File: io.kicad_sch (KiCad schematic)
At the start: 39 parts, among them J10 RIGHT WHEEL SENS, J11 STARTER CON, J12 USB_C_Receptacle, J13 USB_C_Receptacle, J14 CAN, J15 3.3V OUT, J16 5V OUT, J17 7.5V OUT, J18 OIL CON, J19 IAT CON, J20 PRIM TRIGG CON, J21 SEC TRIGG CON, J22 EGT CON, J23 DATA LOGGER CON, J24 IGN CON, J25 INJ CON, J26 MAP, J27 CLT CON, J3 EMU_BLACK_A, J4 EMU_BLACK_B, J6 INJ_&_STARTER, J7 16V OUT, J8 SERVO, J9 LEFT WHEEL SENS, K1 FINDER-34.51 INJ, K2 FINDER-34.51 STARTER, K3 FINDER-34.51 INJ, Q2 IRFP1405PBF, Q3 IRFP1405PBF, Q4 IRFP1405PBF, U7 TXS0108EPWR, U8 2EDN7524F

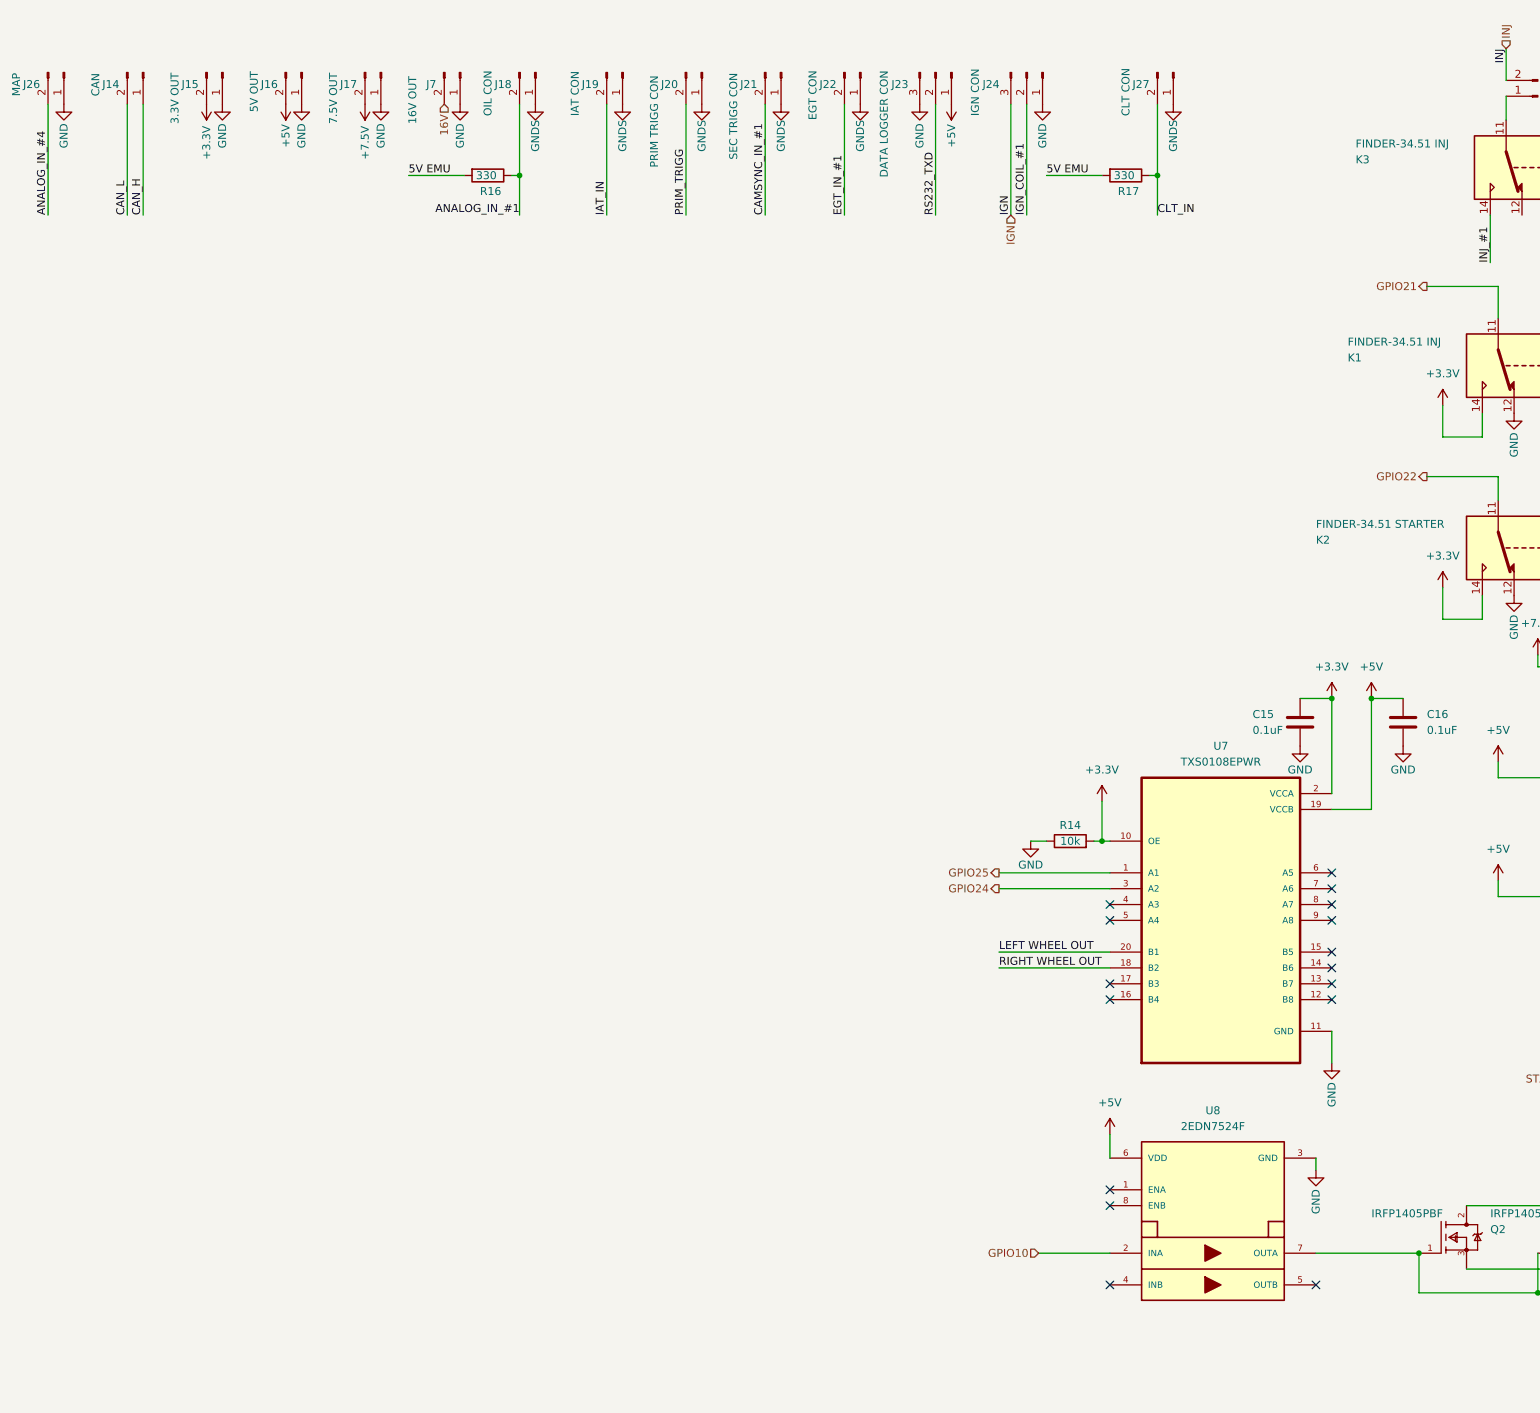
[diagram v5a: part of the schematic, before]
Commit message: Added CAN transsiver to RP2040
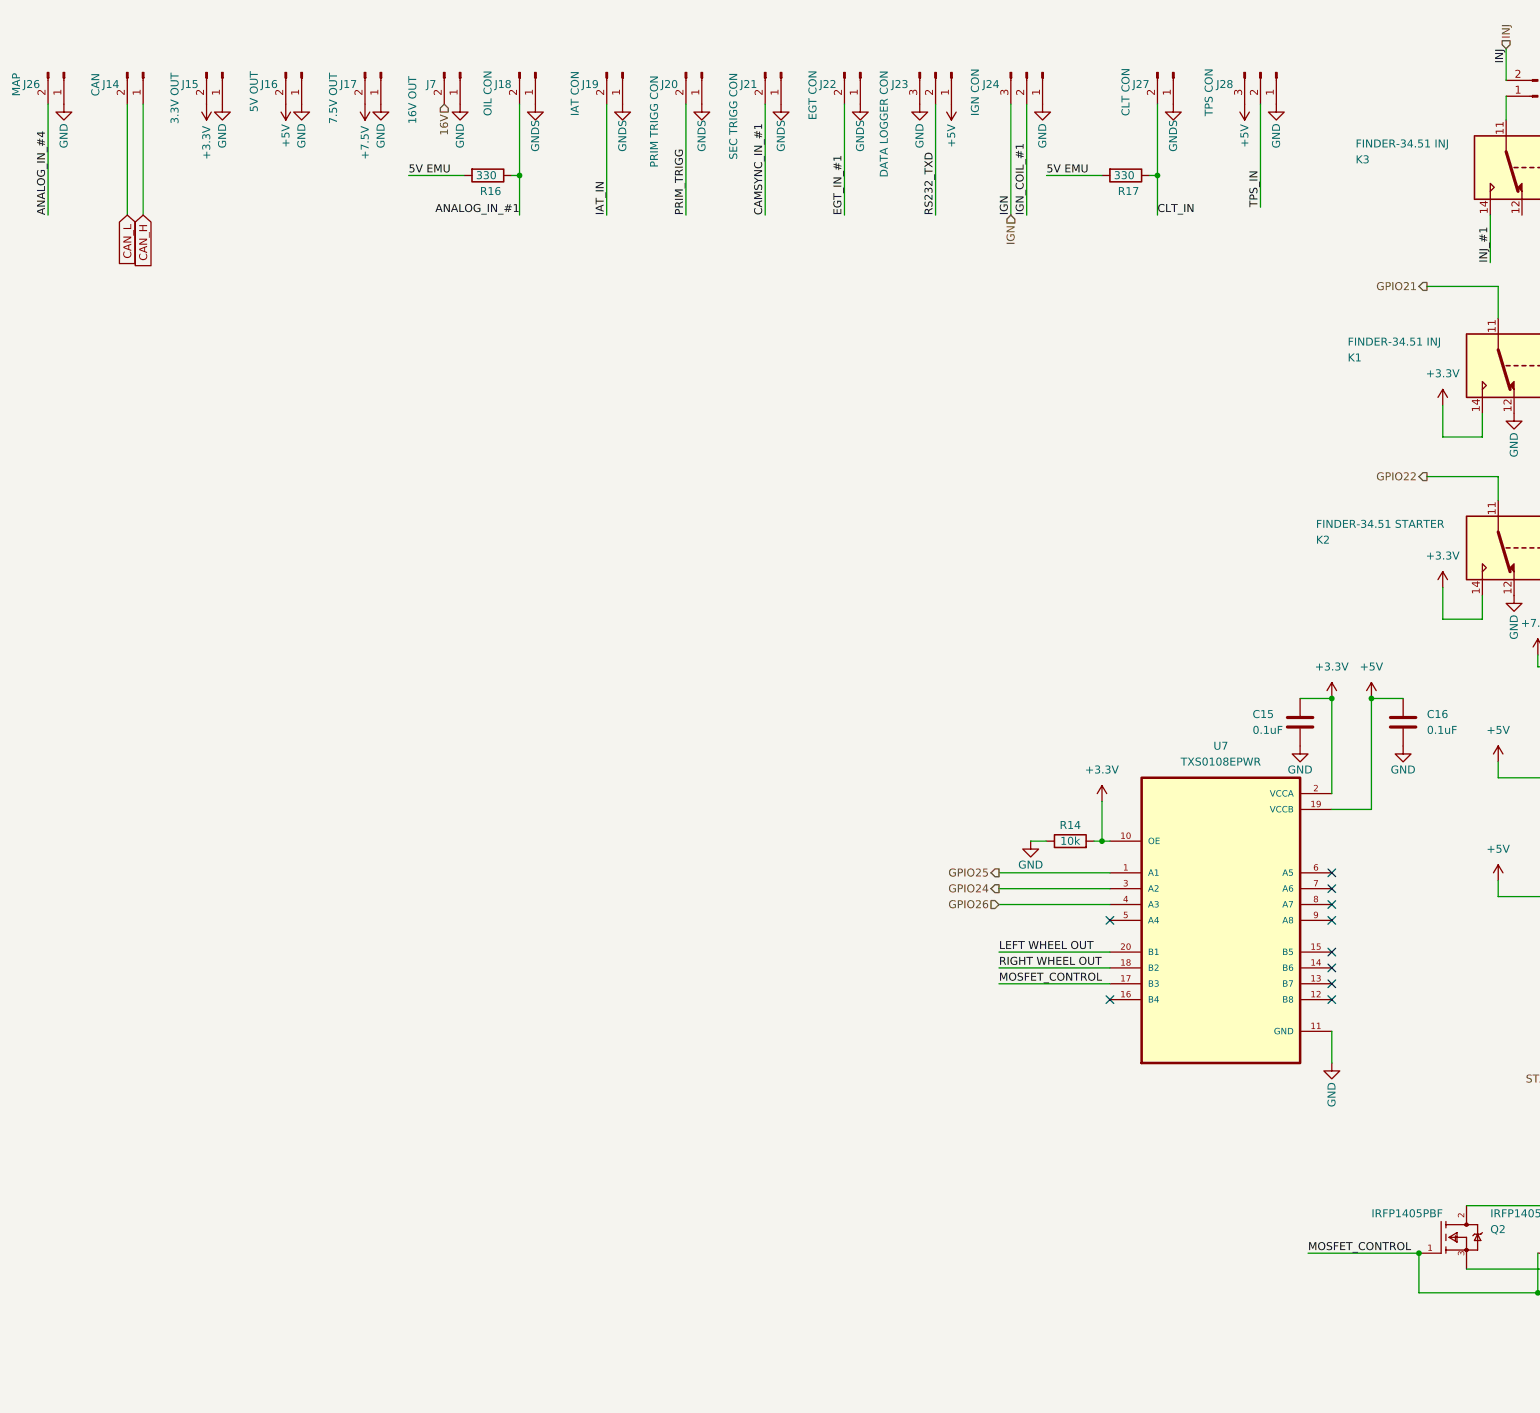
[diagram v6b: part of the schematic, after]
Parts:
- removed U8: 2EDN7524F, 2EDN7524F:SOIC127P600X175-8N-22-V, symbol 2EDN7524F:2EDN7524F
- added J28: TPS CON, TerminalBlock_Phoenix:TerminalBlock_Phoenix_MPT-0,5-3-2.54_1x03_P2.54mm_Horizontal, symbol Connector:Conn_01x03_Male
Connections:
- net +5V: now also J28.3 (Pin_3)
- net GND: now also J28.1 (Pin_1)
- net TPS_IN: now also J28.2 (Pin_2)
- net MOSFET_CONTROL: now reaches U7.17 (B3)
- net MOSFET_CONTROL: now also Q2.1 (G), Q3.1 (G), Q4.1 (G)
- net GPIO26: now reaches U7.4 (A3)
- no-connect marks 42 -> 36
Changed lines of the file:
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@@
   (no_connect (at 46.99 154.94))
   (no_connect (at 46.99 213.36))
-  (no_connect (at 290.83 214.63))
   (no_connect (at 46.99 144.78))
   (no_connect (at 290.83 168.91))
@@
   (no_connect (at 290.83 156.21))
   (no_connect (at 46.99 152.4))
-  (no_connect (at 323.85 214.63))
   (no_connect (at 46.99 147.32))
   (no_connect (at 46.99 139.7))
-  (no_connect (at 290.83 166.37))
   (no_connect (at 46.99 180.34))
   (no_connect (at 46.99 231.14))
   (no_connect (at 326.39 161.29))
-  (no_connect (at 290.83 201.93))
-  (no_connect (at 290.83 199.39))
   (no_connect (at 375.92 189.23))
   (no_connect (at 46.99 137.16))
-  (no_connect (at 290.83 153.67))
   (no_connect (at 326.39 166.37))
   (wire (pts (xy 102.87 68.58) (xy 102.87 50.8))
@@
     (stroke (width 0) (type default) (color 0 0 0 0))
   )
-  (wire (pts (xy 279.4 209.55) (xy 290.83 209.55))
-    (stroke (width 0) (type default) (color 0 0 0 0))
-  )
   (wire (pts (xy 54.61 68.58) (xy 54.61 50.8))
     (stroke (width 0) (type default) (color 0 0 0 0))
@@
     (stroke (width 0) (type default) (color 0 0 0 0))
   )
+  (wire (pts (xy 273.05 166.37) (xy 290.83 166.37))
+    (stroke (width 0) (type default) (color 0 0 0 0))
+  )
   (wire (pts (xy 90.17 20.32) (xy 90.17 38.1))
     (stroke (width 0) (type default) (color 0 0 0 0))
@@
     (stroke (width 0) (type default) (color 0 0 0 0))
   )
-  (wire (pts (xy 323.85 209.55) (xy 340.36 209.55))
+  (wire (pts (xy 322.58 209.55) (xy 340.36 209.55))
     (stroke (width 0) (type default) (color 0 0 0 0))
   )
@@
     (stroke (width 0) (type default) (color 0 0 0 0))
   )
+  (wire (pts (xy 273.05 153.67) (xy 290.83 153.67))
+    (stroke (width 0) (type default) (color 0 0 0 0))
+  )
   (wire (pts (xy 110.49 20.32) (xy 110.49 38.1))
     (stroke (width 0) (type default) (color 0 0 0 0))
@@
     (stroke (width 0) (type default) (color 0 0 0 0))
   )
-  (wire (pts (xy 290.83 190.5) (xy 290.83 194.31))
-    (stroke (width 0) (type default) (color 0 0 0 0))
-  )
   (wire (pts (xy 46.99 114.3) (xy 46.99 116.84))
     (stroke (width 0) (type default) (color 0 0 0 0))
@@
     (stroke (width 0) (type default) (color 0 0 0 0))
   )
-  (wire (pts (xy 323.85 196.215) (xy 323.85 194.31))
-    (stroke (width 0) (type default) (color 0 0 0 0))
-  )
   (wire (pts (xy 359.41 115.57) (xy 381 115.57))
     (stroke (width 0) (type default) (color 0 0 0 0))
@@
     (stroke (width 0) (type default) (color 0 0 0 0))
   )
+  (wire (pts (xy 314.96 41.91) (xy 314.96 25.4))
+    (stroke (width 0) (type default) (color 0 0 0 0))
+  )
   (wire (pts (xy 178.435 36.83) (xy 187.325 36.83))
     (stroke (width 0) (type default) (color 0 0 0 0))
@@
     (effects (font (size 1.27 1.27)) (justify right bottom))
   )
+  (label "MOSFET_CONTROL" (at 273.05 166.37 0)
+    (effects (font (size 1.27 1.27)) (justify left bottom))
+  )
   (label "RIGHT WHEEL OUT" (at 273.05 163.83 0)
     (effects (font (size 1.27 1.27)) (justify left bottom))
@@
     (effects (font (size 1.27 1.27)) (justify left bottom))
   )
+  (label "TPS_IN" (at 314.96 41.91 90)
+    (effects (font (size 1.27 1.27)) (justify left bottom))
+  )
   (label "5V EMU" (at 280.67 36.83 0)
     (effects (font (size 1.27 1.27)) (justify left bottom))
   )
+  (label "MOSFET_CONTROL" (at 322.58 209.55 0)
+    (effects (font (size 1.27 1.27)) (justify left bottom))
+  )
   (label "EGT_IN_#1" (at 24.13 68.58 90)
     (effects (font (size 1.27 1.27)) (justify left bottom))
@@
     (effects (font (size 1.27 1.27)) (justify left bottom))
   )
-  (label "CAN_H" (at 135.89 43.18 90)
-    (effects (font (size 1.27 1.27)) (justify left bottom))
-  )
   (label "RS232_TXD" (at 46.99 68.58 90)
     (effects (font (size 1.27 1.27)) (justify left bottom))
@@
     (effects (font (size 1.27 1.27)) (justify right bottom))
   )
-  (label "CAN_L" (at 133.35 43.18 90)
-    (effects (font (size 1.27 1.27)) (justify left bottom))
-  )
   (label "AUX_#4{slash}Tacho" (at 100.33 68.58 90)
     (effects (font (size 1.27 1.27)) (justify left bottom))
@@
   (label "5V EMU" (at 36.83 20.32 270)
     (effects (font (size 1.27 1.27)) (justify right bottom))
+  )
+  (global_label "CAN_H" (shape input) (at 135.89 43.18 270) (fields_autoplaced)
+    (effects (font (size 1.27 1.27)) (justify right))
+    (property "Intersheet References" "${INTERSHEET_REFS}" (id 0) (at 135.9694 51.5802 90)
+      (effects (font (size 1.27 1.27)) (justify right) hide)
+    )
+  )
+  (global_label "CAN_L" (shape input) (at 133.35 43.18 270) (fields_autoplaced)
+    (effects (font (size 1.27 1.27)) (justify right))
+    (property "Intersheet References" "${INTERSHEET_REFS}" (id 0) (at 133.4294 51.2779 90)
+      (effects (font (size 1.27 1.27)) (justify right) hide)
+    )
   )
   (hierarchical_label "EMU" (shape input) (at 52.07 68.58 270)
@@
     (effects (font (size 1.27 1.27)) (justify right))
   )
-  (hierarchical_label "GPIO10" (shape input) (at 279.4 209.55 180)
-    (effects (font (size 1.27 1.27)) (justify right))
-  )
   (hierarchical_label "16V" (shape input) (at 184.15 25.4 270)
     (effects (font (size 1.27 1.27)) (justify right))
@@
     (effects (font (size 1.27 1.27)) (justify right))
   )
+  (hierarchical_label "GPIO26" (shape input) (at 273.05 153.67 180)
+    (effects (font (size 1.27 1.27)) (justify right))
+  )
   (hierarchical_label "GPIO22" (shape output) (at 341.63 85.09 180)
     (effects (font (size 1.27 1.27)) (justify right))
@@
     )
     (pin "1")
+  )
+  (symbol (lib_id "Connector:Conn_01x03_Male") (at 314.96 20.32 270) (unit 1)
+    (in_bom yes) (on_board yes)
+    (property "Reference" "J28" (id 0) (at 309.245 22.225 90))
+    (property "Value" "TPS CON" (id 1) (at 306.705 23.495 0))
+    (property "Footprint" "TerminalBlock_Phoenix:TerminalBlock_Phoenix_MPT-0,5-3-2.54_1x03_P2.54mm_Horizontal" (id 2) (at 314.96 20.32 0)
+      (effects (font (size 1.27 1.27)) hide)
+    )
+    (property "Datasheet" "~" (id 3) (at 314.96 20.32 0)
+      (effects (font (size 1.27 1.27)) hide)
+    )
+    (pin "1")
+    (pin "2")
+    (pin "3")
   )
   (symbol (lib_id "TXS0108EPWR:TXS0108EPWR") (at 308.61 156.21 0) (unit 1)
@@
     (pin "2")
   )
-  (symbol (lib_id "2EDN7524F:2EDN7524F") (at 295.91 191.77 0) (unit 1)
-    (in_bom yes) (on_board yes) (fields_autoplaced)
-    (property "Reference" "U8" (id 0) (at 307.34 186.69 0))
-    (property "Value" "2EDN7524F" (id 1) (at 307.34 189.23 0))
-    (property "Footprint" "2EDN7524F:SOIC127P600X175-8N-22-V" (id 2) (at 295.91 191.77 0)
-      (effects (font (size 1.27 1.27)) (justify bottom) hide)
-    )
-    (property "Datasheet" "" (id 3) (at 295.91 191.77 0)
-      (effects (font (size 1.27 1.27)) hide)
-    )
-    (pin "1")
-    (pin "2")
-    (pin "3")
-    (pin "4")
-    (pin "5")
-    (pin "6")
-    (pin "7")
-    (pin "8")
-  )
   (symbol (lib_id "power:GNDS") (at 250.825 25.4 0) (unit 1)
     (in_bom yes) (on_board yes)
@@
     (pin "1")
     (pin "2")
+  )
+  (symbol (lib_id "power:+5V") (at 312.42 25.4 180) (unit 1)
+    (in_bom yes) (on_board yes)
+    (property "Reference" "#PWR0153" (id 0) (at 312.42 21.59 0)
+      (effects (font (size 1.27 1.27)) hide)
+    )
+    (property "Value" "+5V" (id 1) (at 312.42 30.48 90))
+    (property "Footprint" "" (id 2) (at 312.42 25.4 0)
+      (effects (font (size 1.27 1.27)) hide)
+    )
+    (property "Datasheet" "" (id 3) (at 312.42 25.4 0)
+      (effects (font (size 1.27 1.27)) hide)
+    )
+    (pin "1")
   )
   (symbol (lib_id "power:GND") (at 148.59 25.4 0) (unit 1)
@@
     (pin "2")
     (pin "3")
-  )
-  (symbol (lib_id "power:GND") (at 323.85 196.215 0) (unit 1)
-    (in_bom yes) (on_board yes)
-    (property "Reference" "#PWR0150" (id 0) (at 323.85 202.565 0)
-      (effects (font (size 1.27 1.27)) hide)
-    )
-    (property "Value" "GND" (id 1) (at 323.85 201.295 90))
-    (property "Footprint" "" (id 2) (at 323.85 196.215 0)
-      (effects (font (size 1.27 1.27)) hide)
-    )
-    (property "Datasheet" "" (id 3) (at 323.85 196.215 0)
-      (effects (font (size 1.27 1.27)) hide)
-    )
-    (pin "1")
   )
   (symbol (lib_id "power:GND") (at 186.69 25.4 0) (unit 1)
@@
     (pin "1")
   )
+  (symbol (lib_id "power:GND") (at 317.5 25.4 0) (unit 1)
+    (in_bom yes) (on_board yes)
+    (property "Reference" "#PWR0154" (id 0) (at 317.5 31.75 0)
+      (effects (font (size 1.27 1.27)) hide)
+    )
+    (property "Value" "GND" (id 1) (at 317.5 30.48 90))
+    (property "Footprint" "" (id 2) (at 317.5 25.4 0)
+      (effects (font (size 1.27 1.27)) hide)
+    )
+    (property "Datasheet" "" (id 3) (at 317.5 25.4 0)
+      (effects (font (size 1.27 1.27)) hide)
+    )
+    (pin "1")
+  )
   (symbol (lib_id "power:+3.3V") (at 289.56 137.16 0) (unit 1)
     (in_bom yes) (on_board yes) (fields_autoplaced)
@@
       (effects (font (size 1.27 1.27)) hide)
     )
-    (pin "1")
-  )
-  (symbol (lib_id "power:+5V") (at 290.83 190.5 0) (unit 1)
-    (in_bom yes) (on_board yes) (fields_autoplaced)
-    (property "Reference" "#PWR037" (id 0) (at 290.83 194.31 0)
-      (effects (font (size 1.27 1.27)) hide)
-    )
-    (property "Value" "+5V" (id 1) (at 290.83 185.42 0))
-    (property "Footprint" "" (id 2) (at 290.83 190.5 0)
-      (effects (font (size 1.27 1.27)) hide)
-    )
-    (property "Datasheet" "" (id 3) (at 290.83 190.5 0)
-      (effects (font (size 1.27 1.27)) hide)
-    )
